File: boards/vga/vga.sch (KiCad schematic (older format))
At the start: 81 parts, among them J1 Conn_02x20_Odd_Even, J2 L77HDE15SD1CH4RHNVGA, Q1 BSS84AK, U1 SN74LV161APW, U10 62256-TSOP, U11 SN74LV161APW, U12 SN74LV161APW, U13 SN74LV244APW, U14 SN74LV20APW, U15 74LV32APWJ, U16 74LV08APWJ, U17 AT28C256-PLCC32, U18 SN74LV273APW, U19 SN74LV273APW, U2 SN74LV161APW, U20 CD74AC151M96, U21 SN74LV157APW, U22 SN74LV10APW, U23 SN74LV74APW, U24 SN74LV00APW, U25 74LV32APWJ, U26 SN74LV21APW, U27 SN74AHC1G86DBVR, U28 74LV32APWJ, U29 74LV08APWJ, U3 SN74LV157APW, U30 SN74LV74APW, U4 SN74LV157APW, U5 SN74LV157APW, U6 SN74LV161APW, U7 SN74LV161APW, U8 SN74LV244APW, U9 62256-TSOP, X1 MXO45HS-3C-25M1750

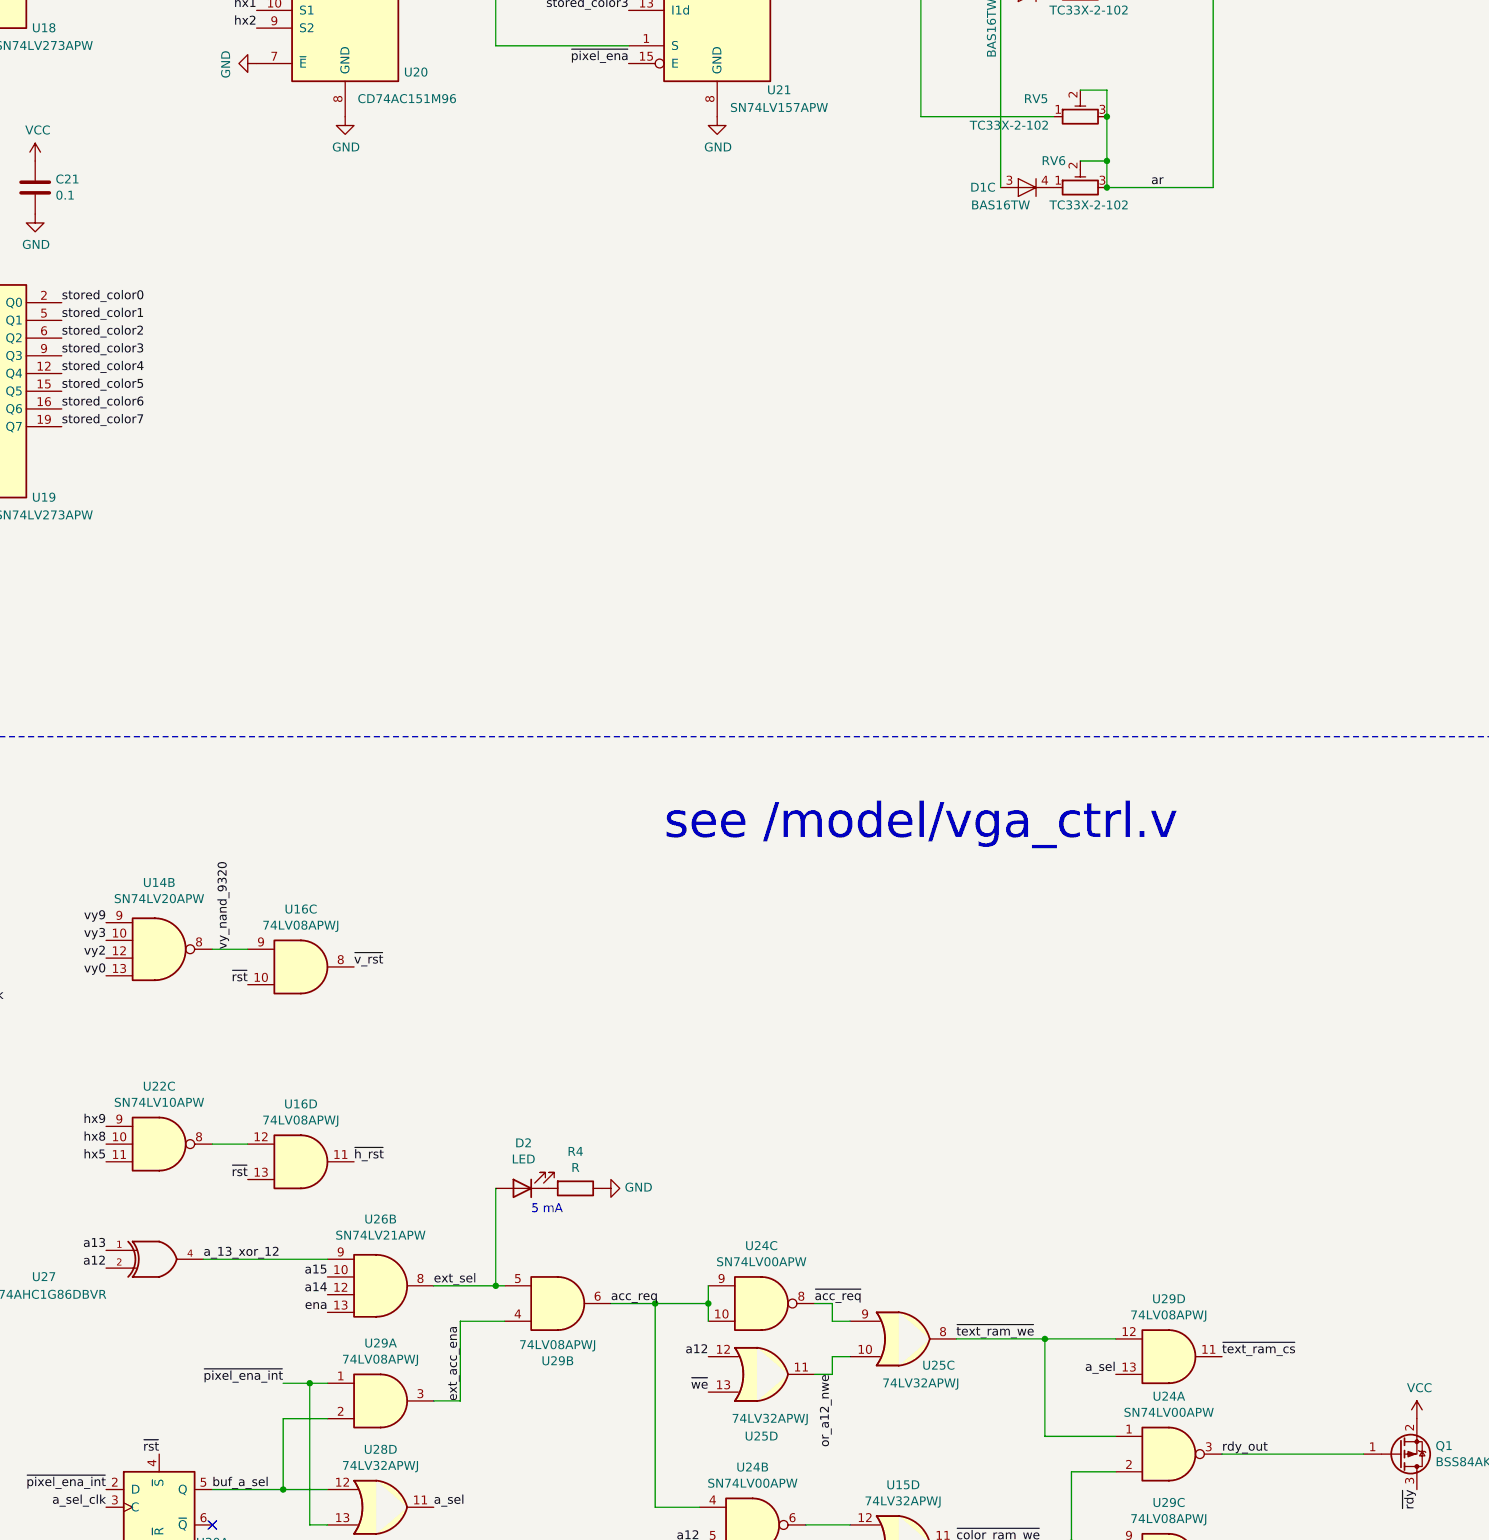
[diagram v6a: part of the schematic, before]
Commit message: VGA: approx board layout
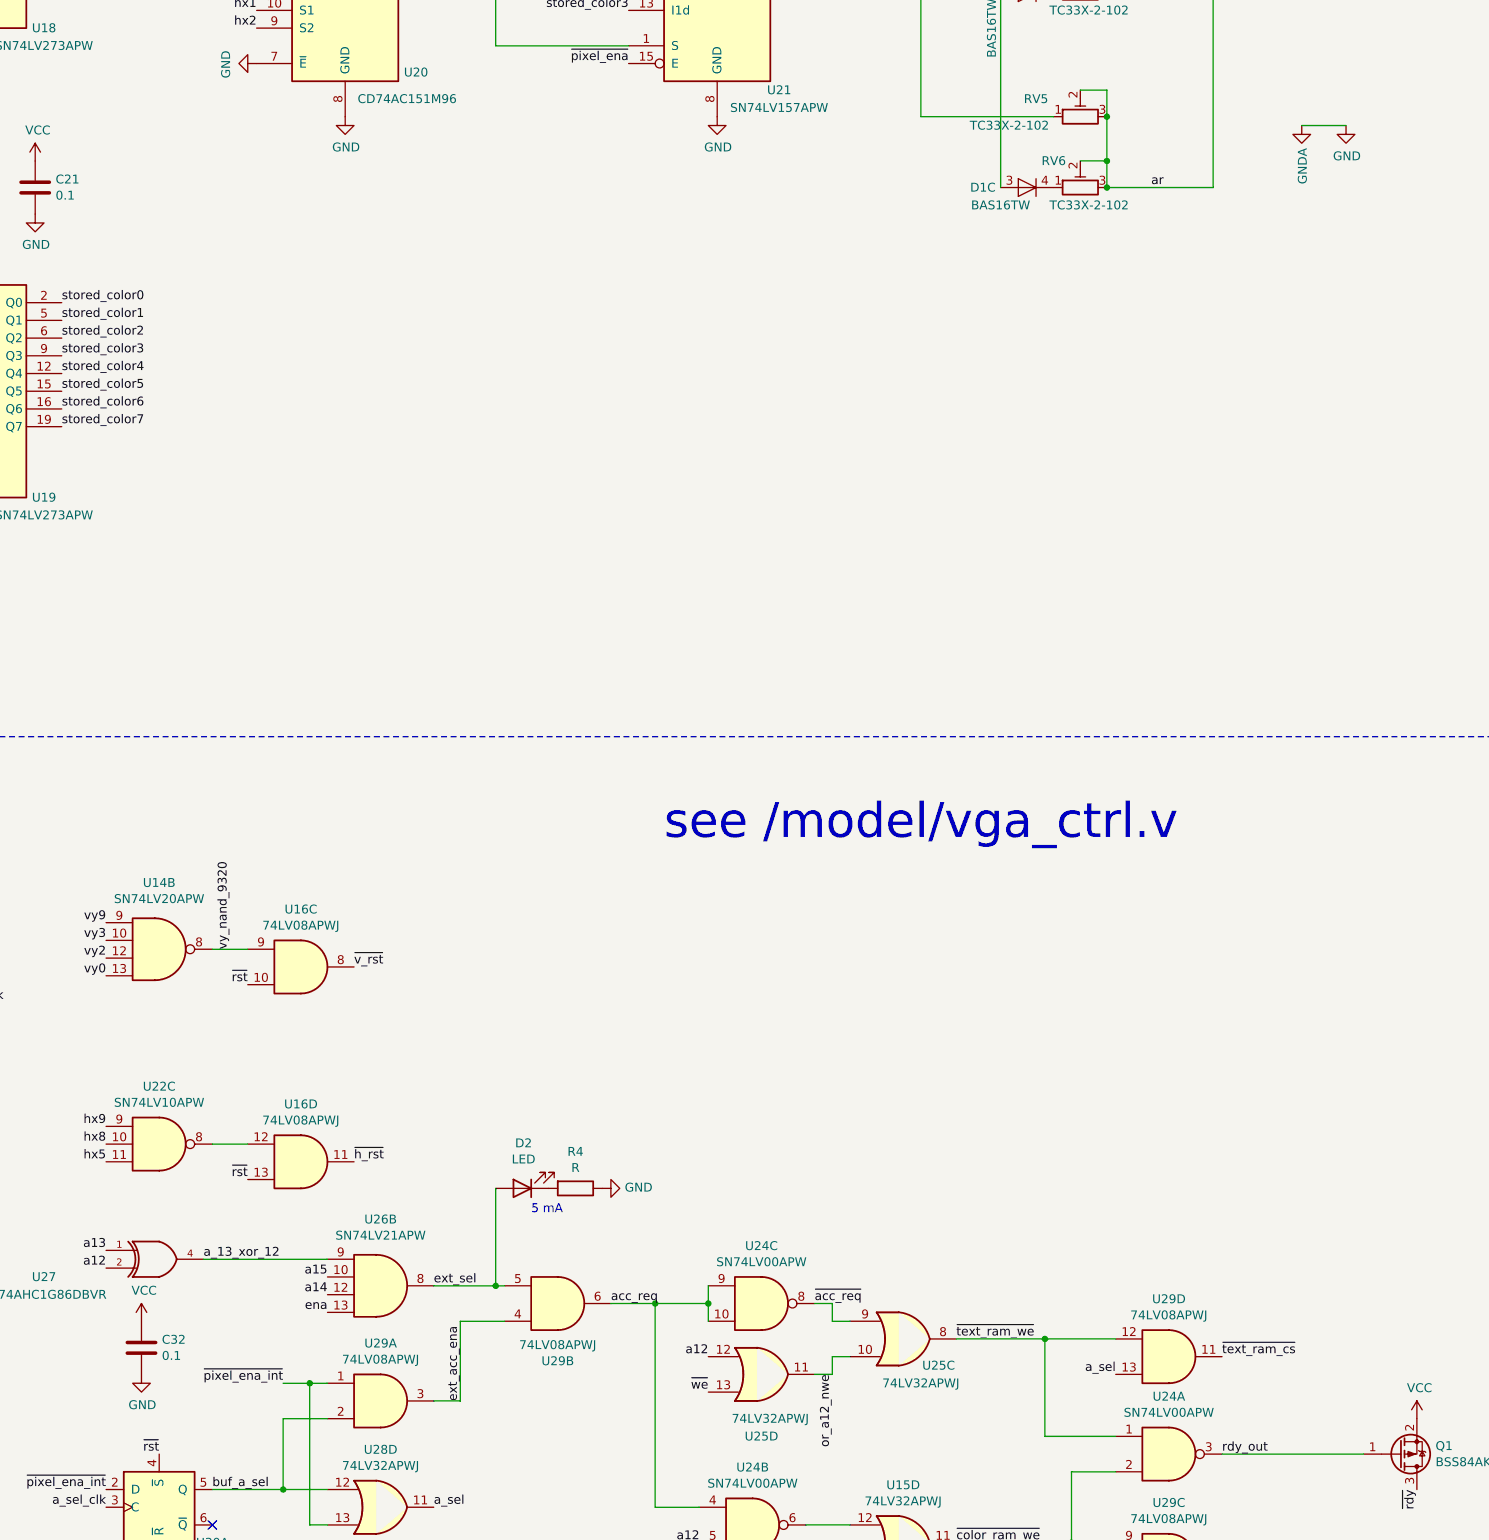
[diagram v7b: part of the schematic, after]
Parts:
- added C32: 0.1, Capacitor_SMD:C_0805_2012Metric, symbol Device:C
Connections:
- net GNDA is gone; now on net GND: J2.6, J2.7, J2.8
- net GND: now also C32.2
- net VCC: now also C32.1
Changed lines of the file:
@@
 Wire Wire Line
 	16700 12300 16700 12850
+Connection ~ 16700 12850
+Wire Wire Line
+	16700 12850 16350 12850
+Text Notes 16900 12450 0    50   ~ 0
+5 mA
+$Comp
+L Device:C C32
+U 1 1 6011F6BA
+P 14700 13200
+F 0 "C32" H 14815 13246 50  0000 L CNN
+F 1 "0.1" H 14815 13155 50  0000 L CNN
+F 2 "Capacitor_SMD:C_0805_2012Metric" H 14738 13050 50  0001 C CNN
+F 3 "~" H 14700 13200 50  0001 C CNN
+	1    14700 13200
+	1    0    0    -1
+$EndComp
+$Comp
+L power:GND #PWR0175
+U 1 1 6011F6C0
+P 14700 13350
+F 0 "#PWR0175" H 14700 13100 50  0001 C CNN
+F 1 "GND" H 14705 13177 50  0000 C CNN
+F 2 "" H 14700 13350 50  0001 C CNN
+F 3 "" H 14700 13350 50  0001 C CNN
+	1    14700 13350
+	1    0    0    -1
+$EndComp
+$Comp
+L power:VCC #PWR0174
+U 1 1 6011F6C6
+P 14700 13050
+F 0 "#PWR0174" H 14700 12900 50  0001 C CNN
+F 1 "VCC" H 14715 13223 50  0000 C CNN
+F 2 "" H 14700 13050 50  0001 C CNN
+F 3 "" H 14700 13050 50  0001 C CNN
+	1    14700 13050
+	1    0    0    -1
+$EndComp
+$Comp
+L power:GNDA #PWR?
+U 1 1 602CF667
+P 21250 6300
+F 0 "#PWR?" H 21250 6050 50  0001 C CNN
+F 1 "GNDA" V 21255 6173 50  0000 R CNN
+F 2 "" H 21250 6300 50  0001 C CNN
+F 3 "" H 21250 6300 50  0001 C CNN
+	1    21250 6300
+	1    0    0    -1
+$EndComp
+$Comp
+L power:GND #PWR?
+U 1 1 602CFE72
+P 21500 6300
+F 0 "#PWR?" H 21500 6050 50  0001 C CNN
+F 1 "GND" H 21505 6127 50  0000 C CNN
+F 2 "" H 21500 6300 50  0001 C CNN
+F 3 "" H 21500 6300 50  0001 C CNN
+	1    21500 6300
+	1    0    0    -1
+$EndComp
+Wire Wire Line
+	21500 6300 21250 6300
 Wire Bus Line
 	11050 5150 11050 5850
@@
 Wire Bus Line
 	6050 4500 6050 10250
-Connection ~ 16700 12850
-Wire Wire Line
-	16700 12850 16350 12850
-Text Notes 16900 12450 0    50   ~ 0
-5 mA
 $EndSCHEMATC

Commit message: VGA board
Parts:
- added R5, R6: 50, Resistor_SMD:R_0805_2012Metric, symbol Device:R
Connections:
- net buf_clk: now also R5.2; no longer U24.11
- net char_a10: now also U10.14 (A3), U9.14 (A3); no longer U10.28 (A10), U9.28 (A10)
- net char_a3: now also U10.28 (A10), U9.28 (A10); no longer U10.14 (A3), U9.14 (A3)
- net hx2: now also R6.2; no longer U1.12 (Q2)
- new net: R6.1, U1.12 (Q2)
- new net ~hx2: R5.1, U24.11
- no-connect marks 25 -> 27
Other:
- moved on the sheet: U24D
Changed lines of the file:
@@
 Text Label 6200 4800 0    50   ~ 0
 char_a2
-Text Label 6200 4900 0    50   ~ 0
+Text Label 6200 5600 0    50   ~ 0
 char_a3
 Text Label 6200 5000 0    50   ~ 0
@@
 Text Label 6200 5500 0    50   ~ 0
 char_a9
-Text Label 6150 5600 0    50   ~ 0
+Text Label 6150 4900 0    50   ~ 0
 char_a10
 Text Label 6150 5700 0    50   ~ 0
@@
 Text Label 6200 8250 0    50   ~ 0
 char_a2
-Text Label 6200 8350 0    50   ~ 0
+Text Label 6200 9050 0    50   ~ 0
 char_a3
 Text Label 6200 8450 0    50   ~ 0
@@
 Text Label 6200 8950 0    50   ~ 0
 char_a9
-Text Label 6150 9050 0    50   ~ 0
+Text Label 6150 8350 0    50   ~ 0
 char_a10
 Text Label 6150 9150 0    50   ~ 0
@@
 P 4800 13500
 F 0 "#PWR021" H 4800 13250 50  0001 C CNN
-F 1 "GND" H 4805 13327 50  0000 C CNN
+F 1 "GND" H 4700 13400 50  0000 C CNN
 F 2 "" H 4800 13500 50  0001 C CNN
 F 3 "" H 4800 13500 50  0001 C CNN
@@
 Text Label 4200 13450 0    50   ~ 0
 hx1
-Text Label 4200 13550 0    50   ~ 0
+Text Label 4500 13550 0    50   ~ 0
 hx2
 Text Label 4200 13650 0    50   ~ 0
@@
 Text Label 13050 11250 0    50   ~ 0
 ~hsync_out
-Text Label 12300 10250 0    50   ~ 0
+Text Label 11950 10250 3    50   ~ 0
 ~hx2
 Text Label 10750 10900 0    50   ~ 0
@@
 L 74xx:74LS00 U24
 U 4 1 5FF2A47A
-P 11950 10250
-F 0 "U24" H 11950 10575 50  0000 C CNN
-F 1 "SN74LV00APW" H 11950 10484 50  0000 C CNN
-F 2 "Package_SO:TSSOP-14_4.4x5mm_P0.65mm" H 11950 10250 50  0001 C CNN
-F 3 "https://www.ti.com/lit/ds/symlink/sn74lv00a.pdf" H 11950 10250 50  0001 C CNN
-	4    11950 10250
+P 11650 10250
+F 0 "U24" H 11650 10575 50  0000 C CNN
+F 1 "SN74LV00APW" H 11650 10484 50  0000 C CNN
+F 2 "Package_SO:TSSOP-14_4.4x5mm_P0.65mm" H 11650 10250 50  0001 C CNN
+F 3 "https://www.ti.com/lit/ds/symlink/sn74lv00a.pdf" H 11650 10250 50  0001 C CNN
+	4    11650 10250
 	1    0    0    -1
 $EndComp
@@
 	12400 12900 12450 12900
 Connection ~ 12400 11150
-Text Label 11550 10250 2    50   ~ 0
+Text Label 11250 10250 2    50   ~ 0
 hx2
 Wire Wire Line
-	11550 10250 11650 10250
+	11250 10250 11350 10250
 Wire Wire Line
-	11650 10250 11650 10150
+	11350 10250 11350 10150
 Wire Wire Line
-	11650 10350 11650 10250
-Connection ~ 11650 10250
+	11350 10350 11350 10250
+Connection ~ 11350 10250
 Wire Wire Line
 	17350 12950 17600 12950
@@
 $EndComp
 $Comp
-L power:GNDA #PWR?
+L power:GNDA #PWR0176
 U 1 1 602CF667
 P 21250 6300
-F 0 "#PWR?" H 21250 6050 50  0001 C CNN
+F 0 "#PWR0176" H 21250 6050 50  0001 C CNN
 F 1 "GNDA" V 21255 6173 50  0000 R CNN
 F 2 "" H 21250 6300 50  0001 C CNN
@@
 $EndComp
 $Comp
-L power:GND #PWR?
+L power:GND #PWR0177
 U 1 1 602CFE72
 P 21500 6300
-F 0 "#PWR?" H 21500 6050 50  0001 C CNN
+F 0 "#PWR0177" H 21500 6050 50  0001 C CNN
 F 1 "GND" H 21505 6127 50  0000 C CNN
 F 2 "" H 21500 6300 50  0001 C CNN
@@
 Wire Wire Line
 	21500 6300 21250 6300
+NoConn ~ 1550 5450
+NoConn ~ 13050 13000
+$Comp
+L Device:R R5
+U 1 1 60AB639B
+P 12100 10250
+F 0 "R5" V 12307 10250 50  0000 C CNN
+F 1 "50" V 12216 10250 50  0000 C CNN
+F 2 "Resistor_SMD:R_0805_2012Metric" V 12030 10250 50  0001 C CNN
+F 3 "~" H 12100 10250 50  0001 C CNN
+	1    12100 10250
+	0    -1   -1   0
+$EndComp
 Wire Bus Line
 	11050 5150 11050 5850
@@
 Wire Bus Line
 	6050 4500 6050 10250
+$Comp
+L Device:R R6
+U 1 1 60AFB465
+P 4350 13550
+F 0 "R6" V 4550 13450 50  0000 C CNN
+F 1 "50" V 4450 13450 50  0000 C CNN
+F 2 "Resistor_SMD:R_0805_2012Metric" V 4280 13550 50  0001 C CNN
+F 3 "~" H 4350 13550 50  0001 C CNN
+	1    4350 13550
+	0    -1   -1   0
+$EndComp
 $EndSCHEMATC
